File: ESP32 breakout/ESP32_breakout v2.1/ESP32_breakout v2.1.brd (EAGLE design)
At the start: 99.1 x 76.2 mm, 37 parts, among them U1 ESP-WROOM-32, U2 NCP-1117, Y1 12MHz

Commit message: Traces
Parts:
- removed U$10: M04, dr-library:1X04
- removed U$2: M102X05, dr-library:2X05
- added U$3: M122ROWS, dr-library:2X06
- R3: device dr-library:RES-0603 -> dr-library:RES-0805
- moved U$1 173.4 mm to (62.2, 5.08), turned to 180 degrees
- moved C8 169.8 mm to (70.5, 22.9)
- moved C7 163.0 mm to (66.7, 22.9), turned to 180 degrees
- moved D1 152.2 mm to (85.1, 29.2), turned to 180 degrees
- moved R2 148.8 mm to (26.7, 8.89), turned to 90 degrees
- moved R1 147.8 mm to (29.2, 8.89), turned to 270 degrees
- moved C2 143.3 mm to (58.4, 27.9), turned to 270 degrees
- moved Y1 134.1 mm to (66.0, 19.1)
- moved C3 132.7 mm to (33.0, 15.2)
- moved C4 127.8 mm to (22.9, 15.2), turned to 180 degrees
- moved R3 124.5 mm to (85.1, 31.8), turned to 180 degrees
- moved U$7 117.6 mm to (64.8, 27.9)
- moved U$9 113.1 mm to (41.9, 5.08), turned to 180 degrees
- moved U$8 50.6 mm to (8.89, 19.1)
- moved J1 38.2 mm to (78.7, 5.08), turned to 180 degrees
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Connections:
- net +3V3: no longer U$10.4
- net GND: no longer U$10.3
- net IO0/T1: now also U$3.1; no longer U$2.1
- net IO16: now also U$3.3; no longer U$2.3
- net IO17: now also U$3.4; no longer U$2.4
- net IO18: now also U$3.6; no longer U$2.6
- net IO19: now also U$3.7; no longer U$2.7
- net IO21: now also U$3.8; no longer U$2.8
- net IO22: now also U$3.11; no longer U$2.9
- net IO23: now also U$3.12; no longer U$2.10
- net IO4/T0: now also U$3.2; no longer U$2.2
- net IO5: now also U$3.5; no longer U$2.5
- net RX: now also U$3.9; no longer U$10.1
- net TX: now also U$3.10; no longer U$10.2
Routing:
- net EN: track 0.00 -> 104.9 mm, vias 0 -> 1
- net IO14/T6: track 0.00 -> 102.0 mm, vias 0 -> 1
- net IO4/T0: track 0.00 -> 100.9 mm
- net S_VP: track 0.00 -> 96.8 mm, vias 0 -> 1
- net S_VN: track 0.00 -> 94.7 mm, vias 0 -> 1
- net IO13/T4: track 0.00 -> 89.4 mm, vias 0 -> 1
- net IO27/T7: track 0.00 -> 88.3 mm, vias 0 -> 1
- net IO2/T2: track 0.00 -> 87.5 mm, vias 0 -> 1
- net IO34: track 0.00 -> 86.6 mm, vias 0 -> 1
- net IO35: track 0.00 -> 84.6 mm, vias 0 -> 1
- net IO0/T1: track 0.00 -> 77.9 mm, vias 0 -> 1
- net IO25: track 0.00 -> 73.9 mm, vias 0 -> 1
- net IO12/T5: track 0.00 -> 72.6 mm, vias 0 -> 1
- net IO26: track 0.00 -> 71.9 mm, vias 0 -> 1
- net IO15/T3: track 0.00 -> 69.2 mm, vias 0 -> 1
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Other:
- board size 99.1 x 76.2 mm -> 88.9 x 83.8 mm
- board text added: "TEXT"

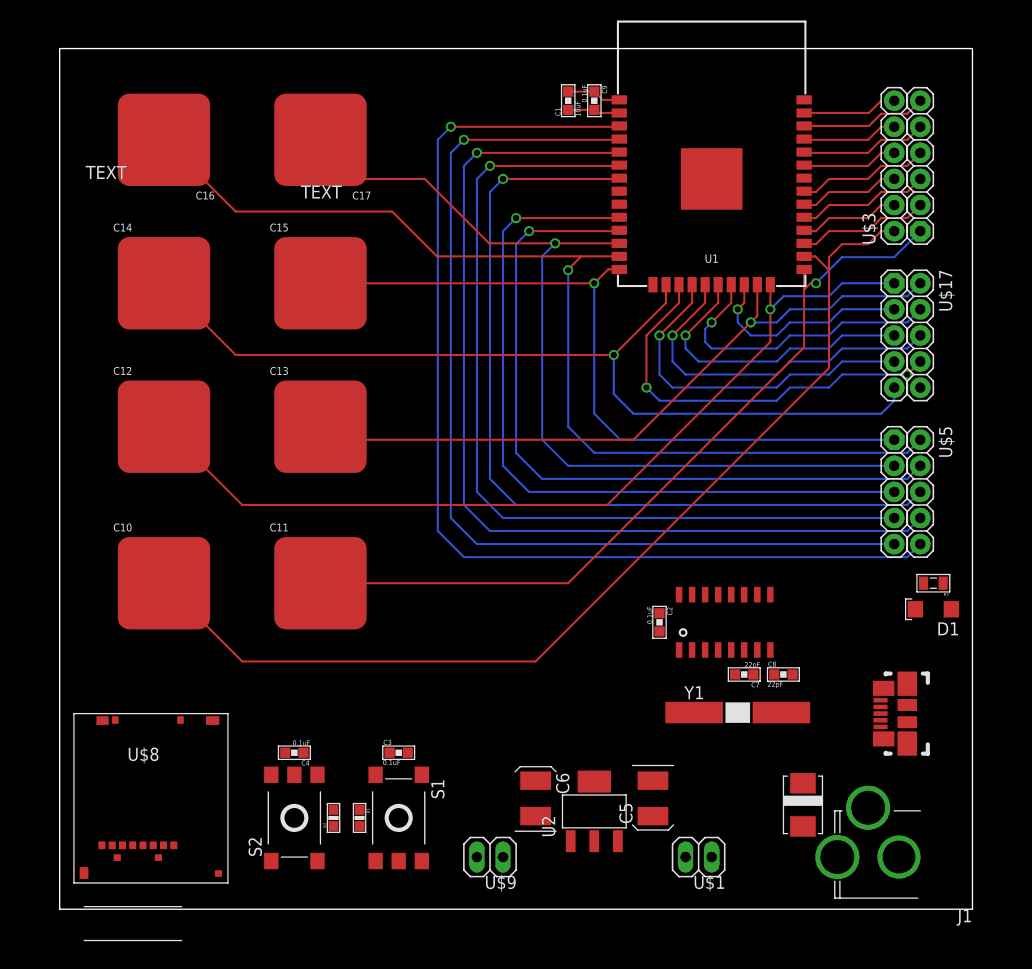
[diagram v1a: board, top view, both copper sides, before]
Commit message: Added more status LEDs
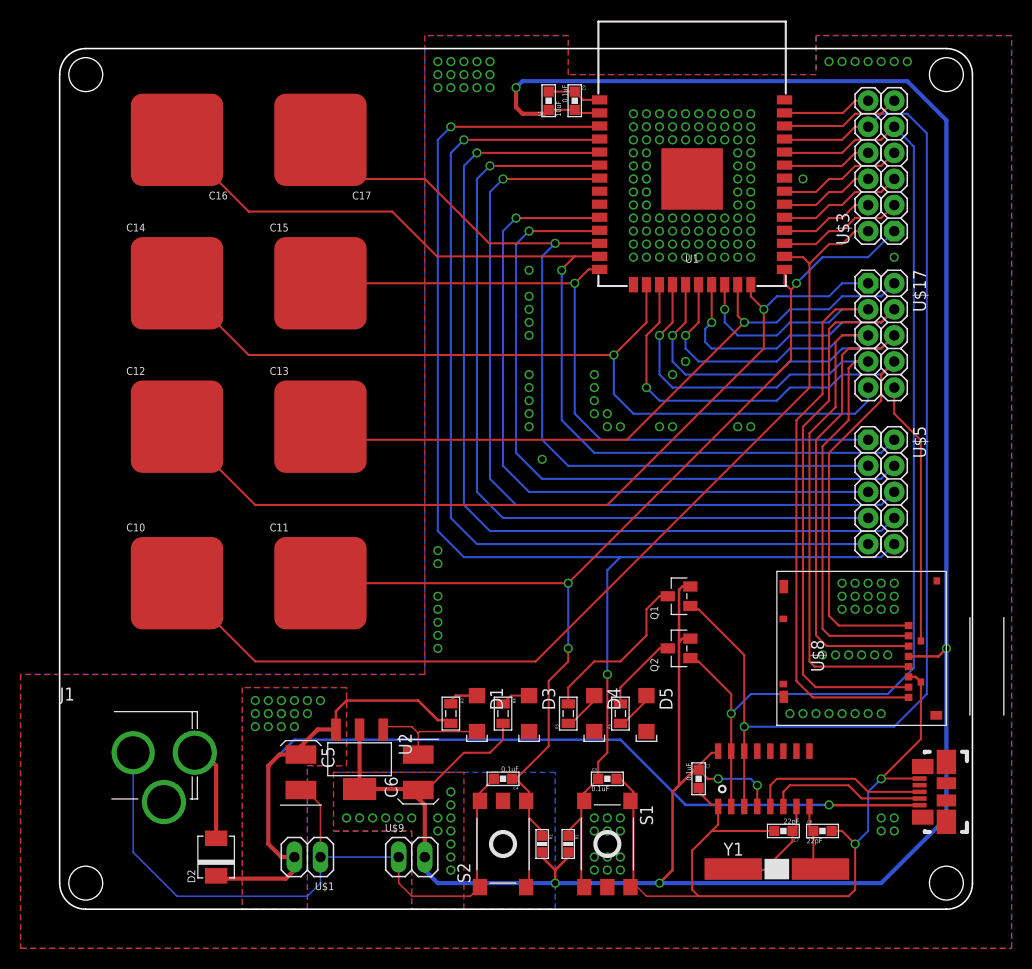
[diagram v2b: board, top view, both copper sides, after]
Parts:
- added D3, D4, D5: (no value), dr-library:LED-1206
- added Q1, Q2: BSS84, dr-library:SOT-23-3
- added R4, R5, R6: 330, dr-library:RES-0805
- added U$10, U$11, U$2, U$6: (no value), EmbeddedAdventures 3:STAND-OFF-HOLE
- D2: value DIODE-10BQ015PBF -> VS-10BQ030-M3; device EmbeddedAdventures 3:10BQ015PB -> dr-library:DO-214AA
- moved J1 69.3 mm to (10.2, 15.2), turned to 0 degrees
- moved U$8 61.3 mm to (69.8, 25.4), turned to 90 degrees
- moved D2 57.4 mm to (15.2, 5.08), turned to 90 degrees
- moved R3 48.7 mm to (38.1, 19.1), turned to 270 degrees
- moved D1 45.6 mm to (40.6, 19.1), turned to 270 degrees
- moved U$1 38.1 mm to (24.1, 5.08)
- moved C5 34.4 mm to (23.5, 13.3), turned to 270 degrees
- moved U2 23.4 mm to (29.2, 14.6), turned to 180 degrees
- moved C3 20.5 mm to (53.3, 12.7)
- moved C4 20.5 mm to (43.2, 12.7)
- moved R1 20.5 mm to (49.5, 6.35)
- moved R2 20.5 mm to (47.0, 6.35), turned to 270 degrees
- moved S1 20.5 mm to (53.3, 6.35)
- moved S2 20.5 mm to (43.2, 6.35)
- moved U$7 15.7 mm to (68.6, 12.7)
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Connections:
- net N$5 renamed D+
- net N$6 renamed D-
- new net N$11: D5.A, R6.1
- new net N$5: D3.A, R4.1
- new net N$6: Q1.D, R5.2
- new net N$7: Q2.D, R6.2
- new net N$8: D4.A, R5.1
- net +3V3: now also Q1.S, Q2.S, R4.2
- net GND: now also D3.C, D4.C, D5.C
- net RX: now also Q2.G
- net TX: now also Q1.G
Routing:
- net +3V3: track 5.09 -> 263.8 mm, vias 0 -> 21
- net GND: track 5.31 -> 197.7 mm, vias 0 -> 192
- net VCC: track 0.00 -> 120.7 mm, vias 0 -> 16
- net TX: track 9.34 -> 111.4 mm, vias 0 -> 1
- net RX: track 12.4 -> 101.2 mm, vias 0 -> 1
- net SD1: track 20.8 -> 71.7 mm
- net SD0: track 29.4 -> 78.7 mm
- net CLK: track 29.4 -> 71.6 mm
- net CMD: track 35.0 -> 75.4 mm
- net SD3: track 34.5 -> 68.5 mm
- net IO0/T1: track 77.9 -> 111.8 mm, vias 1 -> 3
- net SD2: track 40.1 -> 72.3 mm, vias 2 -> 1
- net EN: track 104.9 -> 136.6 mm, vias 1 -> 2
- net D+: track 0.00 -> 17.4 mm
- net N$6: track 0.00 -> 16.5 mm
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- added copper zone on layer 1, net +3V3
- added copper zone on layer 16, net +3V3
- added copper zone on layer 1, net GND
- added copper zone on layer 16, net GND
- added copper zone on layer 1, net VCC
- added copper zone on layer 16, net VCC
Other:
- outline, holes or cut-outs redrawn
- board text removed: "TEXT"
